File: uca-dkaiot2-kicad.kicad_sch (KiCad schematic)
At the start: 5 parts

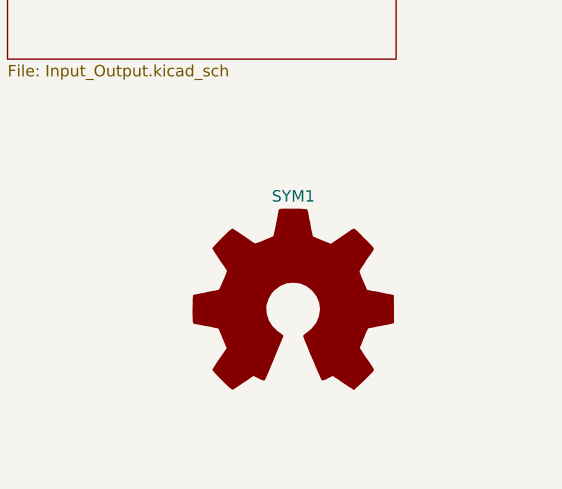
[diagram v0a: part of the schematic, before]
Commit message: OSHW logo tied to ground net
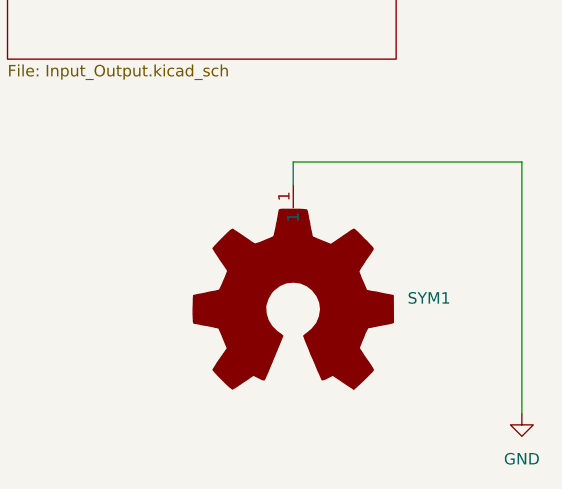
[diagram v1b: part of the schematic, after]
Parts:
- SYM1: symbol Graphic:Logo_Open_Hardware_Large -> Logo_Open_Hardware:Logo_Open_Hardware_Large
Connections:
- new net GND: SYM1.1
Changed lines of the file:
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@@
 		(company "//piernov")
+	)
+	(wire
+		(pts
+			(xy 157.48 128.27) (xy 182.88 128.27)
+		)
+		(stroke
+			(width 0)
+			(type default)
+		)
+	)
+	(wire
+		(pts
+			(xy 157.48 130.81) (xy 157.48 128.27)
+		)
+		(stroke
+			(width 0)
+			(type default)
+		)
+	)
+	(wire
+		(pts
+			(xy 182.88 128.27) (xy 182.88 156.21)
+		)
+		(stroke
+			(width 0)
+			(type default)
+		)
 	)
 	(symbol
@@
 	)
 	(symbol
-		(lib_id "Graphic:Logo_Open_Hardware_Large")
+		(lib_id "Logo_Open_Hardware:Logo_Open_Hardware_Large")
 		(at 157.48 144.78 0)
 		(unit 1)
 		(body_style 1)
-		(exclude_from_sim yes)
+		(exclude_from_sim no)
 		(in_bom no)
 		(on_board yes)
@@
 		(fields_autoplaced yes)
 		(property "Reference" "SYM1"
-			(at 157.48 132.08 0)
-			(show_name no)
-			(do_not_autoplace no)
-			(effects
-				(font
-					(size 1.27 1.27)
-				)
+			(at 170.18 143.421 0)
+			(show_name no)
+			(do_not_autoplace no)
+			(effects
+				(font
+					(size 1.27 1.27)
+				)
+				(justify left)
 			)
 		)
@@
 				)
 			)
+		)
+		(property "Sim.Enable" "0"
+			(at 157.48 144.78 0)
+			(hide yes)
+			(show_name no)
+			(do_not_autoplace no)
+			(effects
+				(font
+					(size 1.27 1.27)
+				)
+			)
+		)
+		(pin "1"
 		)
 		(instances
@@
 					(unit 1)
 				)
+			)
+		)
+	)
+	(symbol
+		(lib_id "power:GND")
+		(at 182.88 156.21 0)
+		(unit 1)
+		(body_style 1)
+		(exclude_from_sim no)
+		(in_bom yes)
+		(on_board yes)
+		(in_pos_files yes)
+		(dnp no)
+		(fields_autoplaced yes)
+		(property "Reference" "#PWR095"
+			(at 182.88 162.56 0)
+			(hide yes)
+			(show_name no)
+			(do_not_autoplace no)
+			(effects
+				(font
+					(size 1.27 1.27)
+				)
+			)
+		)
+		(property "Value" "GND"
+			(at 182.88 161.29 0)
+			(show_name no)
+			(do_not_autoplace no)
+			(effects
+				(font
+					(size 1.27 1.27)
+				)
+			)
+		)
+		(property "Footprint" ""
+			(at 182.88 156.21 0)
+			(hide yes)
+			(show_name no)
+			(do_not_autoplace no)
+			(effects
+				(font
+					(size 1.27 1.27)
+				)
+			)
+		)
+		(property "Datasheet" ""
+			(at 182.88 156.21 0)
+			(hide yes)
+			(show_name no)
+			(do_not_autoplace no)
+			(effects
+				(font
+					(size 1.27 1.27)
+				)
+			)
+		)
+		(property "Description" "Power symbol creates a global label with name \"GND\" , ground"
+			(at 182.88 156.21 0)
+			(hide yes)
+			(show_name no)
+			(do_not_autoplace no)
+			(effects
+				(font
+					(size 1.27 1.27)
+				)
+			)
+		)
+		(pin "1"
+		)
+		(instances
+			(project "uca-dkaiot2-kicad"
+				(path "/13b7de53-ecff-4b32-b513-b5b471d022a3"
+					(reference "#PWR095")
+					(unit 1)
+				)
